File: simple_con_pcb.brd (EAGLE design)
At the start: 39.4 x 16.5 mm, 2 parts

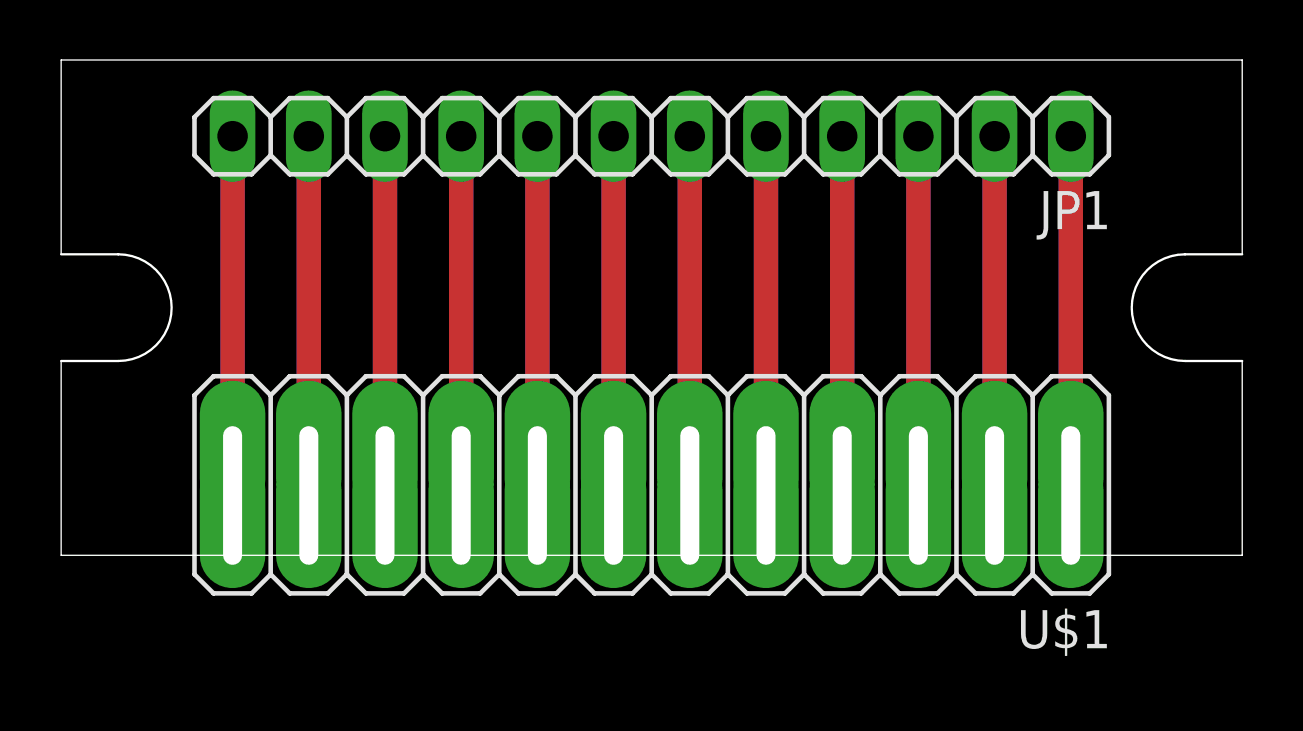
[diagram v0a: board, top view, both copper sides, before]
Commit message: New PCB Rev
Moved holes for ribbon cable 0.050" inward to make soldering easier. There will be less of an issue trying to get the ribbon to lay perfect in order to get the cover on.
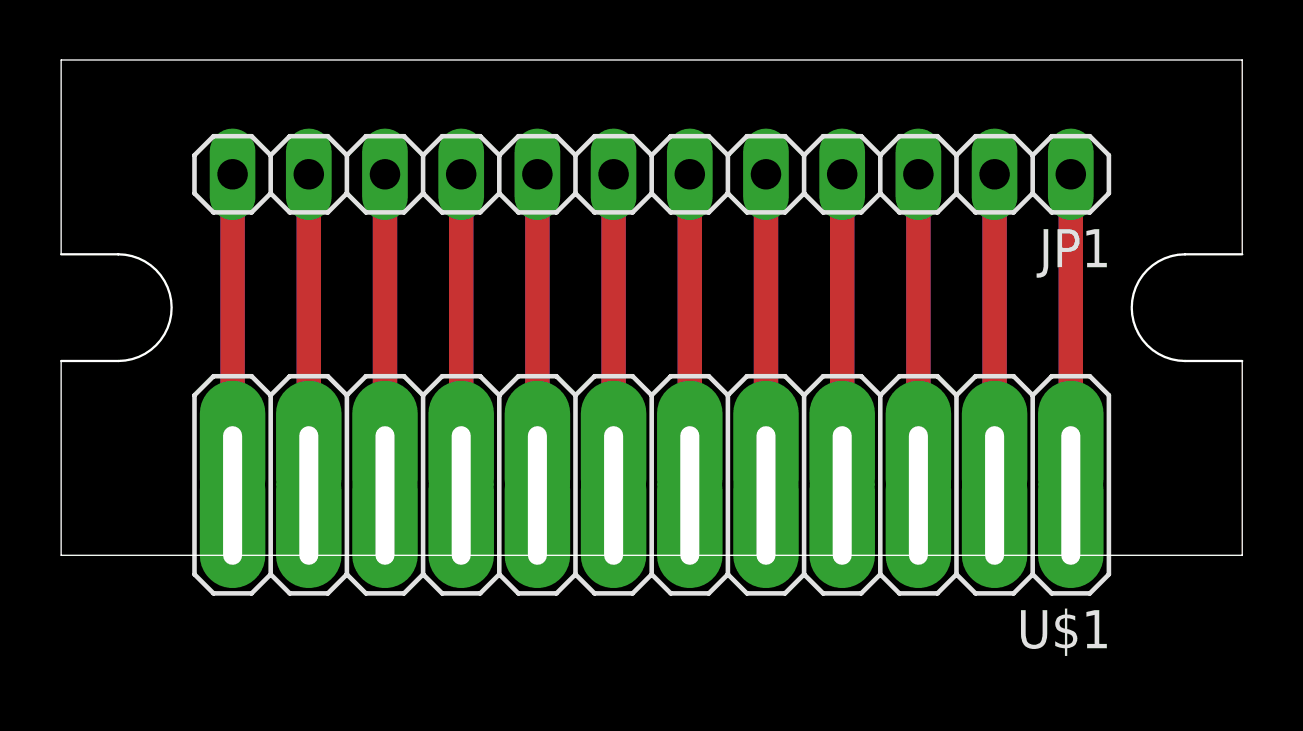
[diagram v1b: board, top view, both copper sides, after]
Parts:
- moved JP1 1.27 mm to (19.7, 12.7)
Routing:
- net N$9: track 27.9 -> 25.4 mm
- net N$8: track 27.9 -> 25.4 mm
- net N$7: track 27.9 -> 25.4 mm
- net N$6: track 27.9 -> 25.4 mm
- net N$5: track 27.9 -> 25.4 mm
- net N$4: track 27.9 -> 25.4 mm
- net N$3: track 27.9 -> 25.4 mm
- net N$2: track 27.9 -> 25.4 mm
- net N$12: track 27.9 -> 25.4 mm
- net N$11: track 27.9 -> 25.4 mm
- net N$10: track 27.9 -> 25.4 mm
- net N$1: track 27.9 -> 25.4 mm
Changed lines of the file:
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@@
 </autorouter>
 <elements>
-<element name="JP1" library="pinhead" package="1X12" value="" x="19.685" y="13.97" smashed="yes" rot="R180">
-<attribute name="NAME" x="35.0012" y="12.1412" size="1.27" layer="25" ratio="10" rot="R180"/>
-<attribute name="VALUE" x="34.925" y="17.145" size="1.27" layer="27" rot="R180"/>
+<element name="JP1" library="pinhead" package="1X12" value="" x="19.685" y="12.7" smashed="yes" rot="R180">
+<attribute name="NAME" x="35.0012" y="10.8712" size="1.27" layer="25" ratio="10" rot="R180"/>
+<attribute name="VALUE" x="34.925" y="15.875" size="1.27" layer="27" rot="R180"/>
 </element>
 <element name="U$1" library="pinhead" package="1X12_SLOT" value="12PINSLOT" x="19.685" y="0" smashed="yes" rot="R180">
@@
 <contactref element="JP1" pad="1"/>
 <contactref element="U$1" pad="1"/>
-<wire x1="33.655" y1="0" x2="33.655" y2="13.97" width="0.8128" layer="1"/>
-<wire x1="33.655" y1="0" x2="33.655" y2="13.97" width="0.8128" layer="16"/>
+<wire x1="33.655" y1="0" x2="33.655" y2="12.7" width="0.8128" layer="1"/>
+<wire x1="33.655" y1="0" x2="33.655" y2="12.7" width="0.8128" layer="16"/>
 <contactref element="U$1" pad="P$1"/>
 <wire x1="33.655" y1="0" x2="33.655" y2="2.54" width="0" layer="19" extent="1-1"/>
@@
 <contactref element="JP1" pad="2"/>
 <contactref element="U$1" pad="2"/>
-<wire x1="31.115" y1="0" x2="31.115" y2="13.97" width="0.8128" layer="1"/>
-<wire x1="31.115" y1="0" x2="31.115" y2="13.97" width="0.8128" layer="16"/>
+<wire x1="31.115" y1="0" x2="31.115" y2="12.7" width="0.8128" layer="1"/>
+<wire x1="31.115" y1="0" x2="31.115" y2="12.7" width="0.8128" layer="16"/>
 <contactref element="U$1" pad="P$2"/>
 <wire x1="31.115" y1="0" x2="31.115" y2="2.54" width="0" layer="19" extent="1-1"/>
@@
 <contactref element="JP1" pad="3"/>
 <contactref element="U$1" pad="3"/>
-<wire x1="28.575" y1="0" x2="28.575" y2="13.97" width="0.8128" layer="1"/>
-<wire x1="28.575" y1="0" x2="28.575" y2="13.97" width="0.8128" layer="16"/>
+<wire x1="28.575" y1="0" x2="28.575" y2="12.7" width="0.8128" layer="1"/>
+<wire x1="28.575" y1="0" x2="28.575" y2="12.7" width="0.8128" layer="16"/>
 <contactref element="U$1" pad="P$3"/>
 <wire x1="28.575" y1="0" x2="28.575" y2="2.54" width="0" layer="19" extent="1-1"/>
@@
 <contactref element="JP1" pad="4"/>
 <contactref element="U$1" pad="4"/>
-<wire x1="26.035" y1="0" x2="26.035" y2="13.97" width="0.8128" layer="1"/>
-<wire x1="26.035" y1="0" x2="26.035" y2="13.97" width="0.8128" layer="16"/>
+<wire x1="26.035" y1="0" x2="26.035" y2="12.7" width="0.8128" layer="1"/>
+<wire x1="26.035" y1="0" x2="26.035" y2="12.7" width="0.8128" layer="16"/>
 <contactref element="U$1" pad="P$4"/>
 <wire x1="26.035" y1="0" x2="26.035" y2="2.54" width="0" layer="19" extent="1-1"/>
@@
 <contactref element="JP1" pad="5"/>
 <contactref element="U$1" pad="5"/>
-<wire x1="23.495" y1="0" x2="23.495" y2="13.97" width="0.8128" layer="1"/>
-<wire x1="23.495" y1="0" x2="23.495" y2="13.97" width="0.8128" layer="16"/>
+<wire x1="23.495" y1="0" x2="23.495" y2="12.7" width="0.8128" layer="1"/>
+<wire x1="23.495" y1="0" x2="23.495" y2="12.7" width="0.8128" layer="16"/>
 <contactref element="U$1" pad="P$5"/>
 <wire x1="23.495" y1="0" x2="23.495" y2="2.54" width="0" layer="19" extent="1-1"/>
@@
 <contactref element="JP1" pad="6"/>
 <contactref element="U$1" pad="6"/>
-<wire x1="20.955" y1="0" x2="20.955" y2="13.97" width="0.8128" layer="1"/>
-<wire x1="20.955" y1="0" x2="20.955" y2="13.97" width="0.8128" layer="16"/>
+<wire x1="20.955" y1="0" x2="20.955" y2="12.7" width="0.8128" layer="1"/>
+<wire x1="20.955" y1="0" x2="20.955" y2="12.7" width="0.8128" layer="16"/>
 <contactref element="U$1" pad="P$6"/>
 <wire x1="20.955" y1="0" x2="20.955" y2="2.54" width="0" layer="19" extent="1-1"/>
@@
 <contactref element="JP1" pad="7"/>
 <contactref element="U$1" pad="7"/>
-<wire x1="18.415" y1="0" x2="18.415" y2="13.97" width="0.8128" layer="1"/>
-<wire x1="18.415" y1="0" x2="18.415" y2="13.97" width="0.8128" layer="16"/>
+<wire x1="18.415" y1="0" x2="18.415" y2="12.7" width="0.8128" layer="1"/>
+<wire x1="18.415" y1="0" x2="18.415" y2="12.7" width="0.8128" layer="16"/>
 <contactref element="U$1" pad="P$7"/>
 <wire x1="18.415" y1="0" x2="18.415" y2="2.54" width="0" layer="19" extent="1-1"/>
@@
 <contactref element="JP1" pad="8"/>
 <contactref element="U$1" pad="8"/>
-<wire x1="15.875" y1="0" x2="15.875" y2="13.97" width="0.8128" layer="1"/>
-<wire x1="15.875" y1="0" x2="15.875" y2="13.97" width="0.8128" layer="16"/>
+<wire x1="15.875" y1="0" x2="15.875" y2="12.7" width="0.8128" layer="1"/>
+<wire x1="15.875" y1="0" x2="15.875" y2="12.7" width="0.8128" layer="16"/>
 <contactref element="U$1" pad="P$8"/>
 <wire x1="15.875" y1="0" x2="15.875" y2="2.54" width="0" layer="19" extent="1-1"/>
@@
 <contactref element="JP1" pad="9"/>
 <contactref element="U$1" pad="9"/>
-<wire x1="13.335" y1="0" x2="13.335" y2="13.97" width="0.8128" layer="1"/>
-<wire x1="13.335" y1="0" x2="13.335" y2="13.97" width="0.8128" layer="16"/>
+<wire x1="13.335" y1="0" x2="13.335" y2="12.7" width="0.8128" layer="1"/>
+<wire x1="13.335" y1="0" x2="13.335" y2="12.7" width="0.8128" layer="16"/>
 <contactref element="U$1" pad="P$9"/>
 <wire x1="13.335" y1="0" x2="13.335" y2="2.54" width="0" layer="19" extent="1-1"/>
@@
 <contactref element="JP1" pad="10"/>
 <contactref element="U$1" pad="10"/>
-<wire x1="10.795" y1="0" x2="10.795" y2="13.97" width="0.8128" layer="1"/>
-<wire x1="10.795" y1="0" x2="10.795" y2="13.97" width="0.8128" layer="16"/>
+<wire x1="10.795" y1="0" x2="10.795" y2="12.7" width="0.8128" layer="1"/>
+<wire x1="10.795" y1="0" x2="10.795" y2="12.7" width="0.8128" layer="16"/>
 <contactref element="U$1" pad="P$10"/>
 <wire x1="10.795" y1="0" x2="10.795" y2="2.54" width="0" layer="19" extent="1-1"/>
@@
 <contactref element="JP1" pad="11"/>
 <contactref element="U$1" pad="11"/>
-<wire x1="8.255" y1="0" x2="8.255" y2="13.97" width="0.8128" layer="1"/>
-<wire x1="8.255" y1="0" x2="8.255" y2="13.97" width="0.8128" layer="16"/>
+<wire x1="8.255" y1="0" x2="8.255" y2="12.7" width="0.8128" layer="1"/>
+<wire x1="8.255" y1="0" x2="8.255" y2="12.7" width="0.8128" layer="16"/>
 <contactref element="U$1" pad="P$11"/>
 <wire x1="8.255" y1="0" x2="8.255" y2="2.54" width="0" layer="19" extent="1-1"/>
@@
 <contactref element="JP1" pad="12"/>
 <contactref element="U$1" pad="12"/>
-<wire x1="5.715" y1="0" x2="5.715" y2="13.97" width="0.8128" layer="1"/>
-<wire x1="5.715" y1="0" x2="5.715" y2="13.97" width="0.8128" layer="16"/>
+<wire x1="5.715" y1="0" x2="5.715" y2="12.7" width="0.8128" layer="1"/>
+<wire x1="5.715" y1="0" x2="5.715" y2="12.7" width="0.8128" layer="16"/>
 <contactref element="U$1" pad="P$12"/>
 <wire x1="5.715" y1="0" x2="5.715" y2="2.54" width="0" layer="19" extent="1-1"/>
